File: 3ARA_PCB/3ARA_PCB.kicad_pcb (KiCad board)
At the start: 2 copper layers, 57 parts, among them J1 ST-LINK V2, J10 Encoder 2, J11 Encoder 3, J12 JUMP_1, J13 JUMP_2, J14 SPI 1, J15 UART 5, J2 Motor 1, J3 Hall 1, J4 Motor 2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

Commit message: Avance con el PCB
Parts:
- removed C14: 100nF, Capacitor_SMD:C_0805_2012Metric_Pad1.18x1.45mm_HandSolder
- removed C15: 1uF, Capacitor_SMD:C_0805_2012Metric_Pad1.18x1.45mm_HandSolder
- added C21: 1000uF, Capacitor_THT:CP_Radial_D10.0mm_P7.50mm, F.Cu at (184.1, 70.4)
- added D5: LED, LED_SMD:LED_0805_2012Metric_Pad1.15x1.40mm_HandSolder, F.Cu at (150.6, 78.1)
- added D6: LED, LED_SMD:LED_0805_2012Metric_Pad1.15x1.40mm_HandSolder, F.Cu at (150.6, 72.1)
- added J16: GPIO, Connector_PinHeader_2.54mm:PinHeader_2x05_P2.54mm_Vertical, F.Cu at (169.1, 88.5)
- added J9: DC Input, Connector_JST:JST_EH_B2B-EH-A_1x02_P2.50mm_Vertical, F.Cu at (154.2, 53.8)
- added L2: 100uH - optional, Inductor_THT:L_Axial_L7.0mm_D3.3mm_P12.70mm_Horizontal_Fastron_MICC, F.Cu at (181.1, 65.5)
- added R12: 1K, Resistor_SMD:R_0805_2012Metric_Pad1.20x1.40mm_HandSolder, F.Cu at (185.8, 94.8)
- added R13: 1K, Resistor_SMD:R_0805_2012Metric_Pad1.20x1.40mm_HandSolder, F.Cu at (185.8, 92.5)
- added R14: 1K, Resistor_SMD:R_0805_2012Metric_Pad1.20x1.40mm_HandSolder, F.Cu at (147.9, 72.1)
- C18, C19: value 0.1uF -> 100nF
- J1: footprint Connector_PinHeader_2.54mm:PinHeader_2x05_P2.54mm_Vertical -> Connector_IDC:IDC-Header_2x05_P2.54mm_Vertical
- J14: value SPI 1 -> I2C 1
- J3: value Hall 1 -> Hall 3; footprint Connector_PinHeader_2.54mm:PinHeader_1x03_P2.54mm_Vertical -> Connector_JST:JST_EH_B3B-EH-A_1x03_P2.50mm_Vertical
- J5: footprint Connector_PinHeader_2.54mm:PinHeader_1x03_P2.54mm_Vertical -> Connector_JST:JST_EH_B3B-EH-A_1x03_P2.50mm_Vertical
- J7: value Hall 3 -> Hall 1; footprint Connector_PinHeader_2.54mm:PinHeader_1x03_P2.54mm_Vertical -> Connector_JST:JST_EH_B3B-EH-A_1x03_P2.50mm_Vertical
- L1: footprint Inductor_THT:L_Axial_L7.0mm_D3.3mm_P12.70mm_Horizontal_Fastron_MICC -> Inductor_SMD:L_12x12mm_H6mm
- R1: value 47 -> 120
- moved J11 135.3 mm to (175.2, 141.5)
- moved J8 126.9 mm to (124.9, 141.5)
- moved J2 111.1 mm to (196.3, 109.0), turned to 90 degrees
- moved J14 99.2 mm to (196.3, 94.7), turned to 90 degrees
- moved L1 97.1 mm to (191.7, 59.2), turned to 90 degrees
- moved D4 96.4 mm to (165.9, 73.9), turned to 270 degrees
- moved J15 94.3 mm to (196.3, 79.0), turned to 90 degrees
- moved U2 90.4 mm to (117.8, 64.3)
- moved J10 79.3 mm to (150.0, 141.5), turned to 0 degrees
- moved SW2 73.0 mm to (166.8, 122.2)
- moved C5 68.5 mm to (158.8, 86.9), turned to 45 degrees
- moved J7 65.7 mm to (108.6, 127.8), turned to 270 degrees
- moved C3 65.7 mm to (166.5, 102.7)
- moved J6 64.9 mm to (196.3, 136.9), turned to 90 degrees
- moved J4 63.5 mm to (196.3, 122.5), turned to 90 degrees
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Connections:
- C16 pad 2: /VREF+ -> +3V3
- C17 pad 2: /VREF+ -> +3V3
- J1 pad 1: (no net) -> /NRST
- J1 pad 5: (no net) -> GND
- J1 pad 7: (no net) -> Net-(J1-Pad7)
- J1 pad 8: +3V3 -> (no net)
- J11 pad 2: (no net) -> /TIM3_CH1
- J11 pad 3: (no net) -> /TIM3_CH2
- J14 pad 1: /PB5_SPI_1_MOSI -> +3V3
- J14 pad 2: /PB4_SPI_1_MISO -> /PB7_I2C1_SDA
- J14 pad 3: /PA5_SPI_1_SCK -> /PB6_I2C1_SCL
- J2 pad 3: (no net) -> /MOTOR_1_L
- J3 pad 1: /HALL_1 -> /HALL_3
- J4 pad 2: (no net) -> /MOTOR_2_R
- J4 pad 3: (no net) -> /MOTOR_2_L
- J7 pad 1: /HALL_3 -> /HALL_1
- R1 pad 1: /VREF+ -> Net-(D5-Pad2)
- R1 pad 2: +3V3 -> Net-(J1-Pad7)
- R10 pad 1: /HALL_3 -> /HALL_1
- R8 pad 1: /HALL_1 -> /HALL_3
- U1 pad 1: (no net) -> /MOTOR_2_R
- U1 pad 18: /MOTOR_1_R -> /MOTOR_1_L
- U1 pad 21: /VREF+ -> +3V3
- U1 pad 22: /VREF+ -> +3V3
- U1 pad 29: (no net) -> /MOTOR_1_R
- U1 pad 3: (no net) -> /MOTOR_2_L
- U1 pad 30: /PA5_SPI_1_SCK -> (no net)
- U1 pad 31: (no net) -> /TIM3_CH1
- U1 pad 32: (no net) -> /TIM3_CH2
- U1 pad 38: (no net) -> /PE7
- U1 pad 41: (no net) -> /PE10
- U1 pad 42: (no net) -> /PE11
- U1 pad 51: (no net) -> /PB12
- U1 pad 52: (no net) -> /PB13
- U1 pad 53: (no net) -> /PB14
- U1 pad 90: /PB4_SPI_1_MISO -> (no net)
- U1 pad 91: /PB5_SPI_1_MOSI -> (no net)
- U1 pad 92: (no net) -> /PB6_I2C1_SCL
- U1 pad 93: (no net) -> /PB7_I2C1_SDA
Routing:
- net +3V3: track 0.00 -> 548.3 mm, vias 0 -> 2
- net /NRST: track 0.00 -> 109.8 mm
- net /TIM4_CH2: track 0.00 -> 93.4 mm, vias 0 -> 2
- net /TIM4_CH1: track 0.00 -> 88.6 mm, vias 0 -> 2
- net /MOTOR_3(PWM): track 0.00 -> 81.8 mm
- net /MOTOR_2_R: track 0.00 -> 76.4 mm, vias 0 -> 1
- net /MOTOR_2_L: track 0.00 -> 70.6 mm, vias 0 -> 1
- net /HALL_1: track 0.00 -> 69.3 mm
- net /PB7_I2C1_SDA: track 0.00 -> 66.6 mm, vias 0 -> 2
- net /MOTOR_3_R: track 0.00 -> 64.3 mm, vias 0 -> 2
- net /PC12_UART_5_Tx: track 0.00 -> 61.8 mm, vias 0 -> 2
- net /MOTOR_3_L: track 0.00 -> 60.9 mm, vias 0 -> 2
- net /TIM8_CH2: track 0.00 -> 60.4 mm, vias 0 -> 2
- net /PD2_UART_5_Rx: track 0.00 -> 59.6 mm, vias 0 -> 2
- net /TIM8_CH1: track 0.00 -> 58.5 mm, vias 0 -> 2
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- added copper zone on B.Cu, net GND
- added copper zone on F.Cu, net GND
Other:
- board outline added: 95 x 95 mm

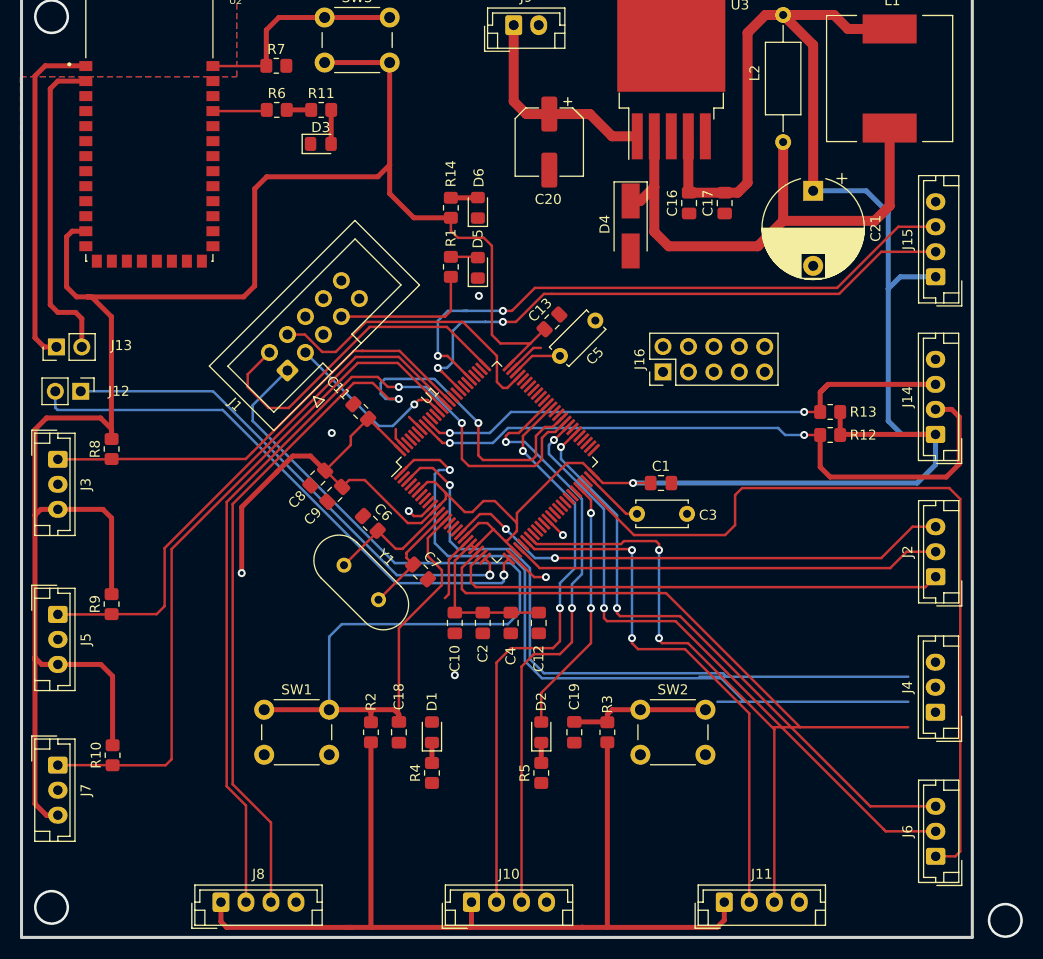
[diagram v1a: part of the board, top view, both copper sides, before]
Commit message: Agregado de gpios a pines
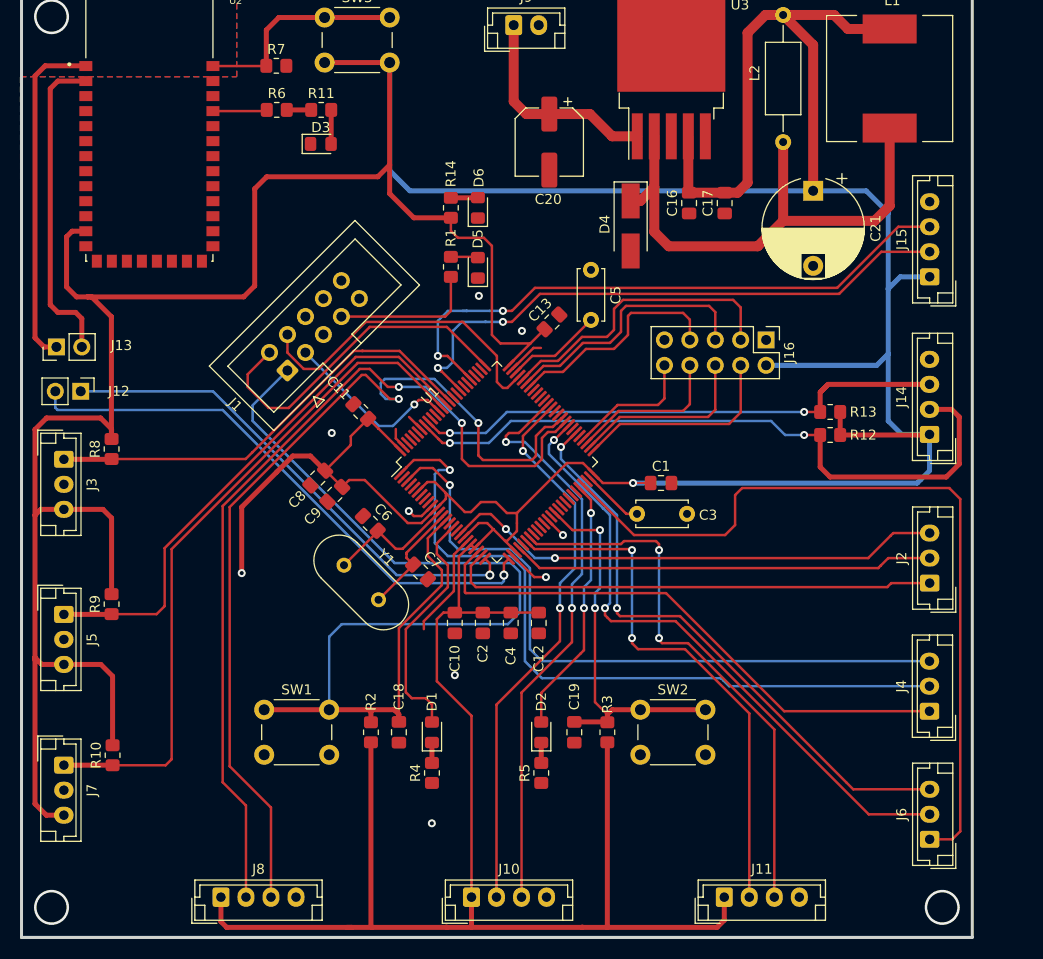
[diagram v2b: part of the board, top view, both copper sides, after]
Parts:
- moved J16 10.8 mm to (179.4, 85.3), turned to 270 degrees
- moved C5 4.75 mm to (161.9, 83.3), turned to 90 degrees
- moved J6 1.80 mm to (195.7, 135.2)
- moved J2 0.87 mm to (195.7, 109.6)
- moved J4 0.61 mm to (195.7, 122.4)
- moved J15 0.60 mm to (195.7, 79.0)
- moved J14 0.60 mm to (195.7, 94.7)
- moved J3 0.60 mm to (109.2, 97.2)
- moved J5 0.60 mm to (109.2, 112.7)
- moved J7 0.60 mm to (109.2, 127.8)
- moved J10 0.50 mm to (150.0, 141.0)
- moved J11 0.50 mm to (175.2, 141.0)
- moved J8 0.50 mm to (124.9, 141.0)
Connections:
- C19 pad 2: /PD15 -> /PE8
- D1 pad 2: /PE0 -> /PC1
- J16 pad 1: /PE7 -> GND
- J16 pad 10: +3V3 -> /PB15
- J16 pad 2: /PE10 -> +3V3
- J16 pad 3: /PE11 -> /PA12
- J16 pad 5: /PB13 -> /PA11
- J16 pad 6: GND -> /PB13
- J16 pad 7: (no net) -> /PA10
- J16 pad 8: (no net) -> /PB14
- J16 pad 9: /PB14 -> GND
- R3 pad 1: /PD15 -> /PE8
- SW2 pad 1: /PD15 -> /PE8
- U1 pad 16: (no net) -> /PC1
- U1 pad 38: /PE7 -> (no net)
- U1 pad 39: (no net) -> /PE8
- U1 pad 41: /PE10 -> (no net)
- U1 pad 42: /PE11 -> (no net)
- U1 pad 54: (no net) -> /PB15
- U1 pad 62: /PD15 -> (no net)
- U1 pad 69: (no net) -> /PA10
- U1 pad 70: (no net) -> /PA11
- U1 pad 71: (no net) -> /PA12
- U1 pad 97: /PE0 -> (no net)
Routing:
- net +3V3: track 548.3 -> 640.5 mm
- net /PE8: track 0.00 -> 38.5 mm, vias 0 -> 2
- net /PA12: track 0.00 -> 29.9 mm
- net /PA11: track 0.00 -> 26.3 mm
- net /PC1: track 0.00 -> 24.3 mm
- net /PA10: track 0.00 -> 22.4 mm
- net /PB12: track 0.00 -> 21.0 mm
- net /PB13: track 0.00 -> 18.5 mm
- net /PB14: track 0.00 -> 15.8 mm
- net /PD15: track 14.1 -> 0.00 mm
- net /PB15: track 0.00 -> 13.1 mm
- net Net-(C5-Pad1): track 5.09 -> 9.68 mm
- net GND: track 23.5 -> 27.5 mm, vias 8 -> 10
- net /TIM8_CH1: track 58.5 -> 55.6 mm
- net /SWDIO: track 29.9 -> 32.4 mm
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
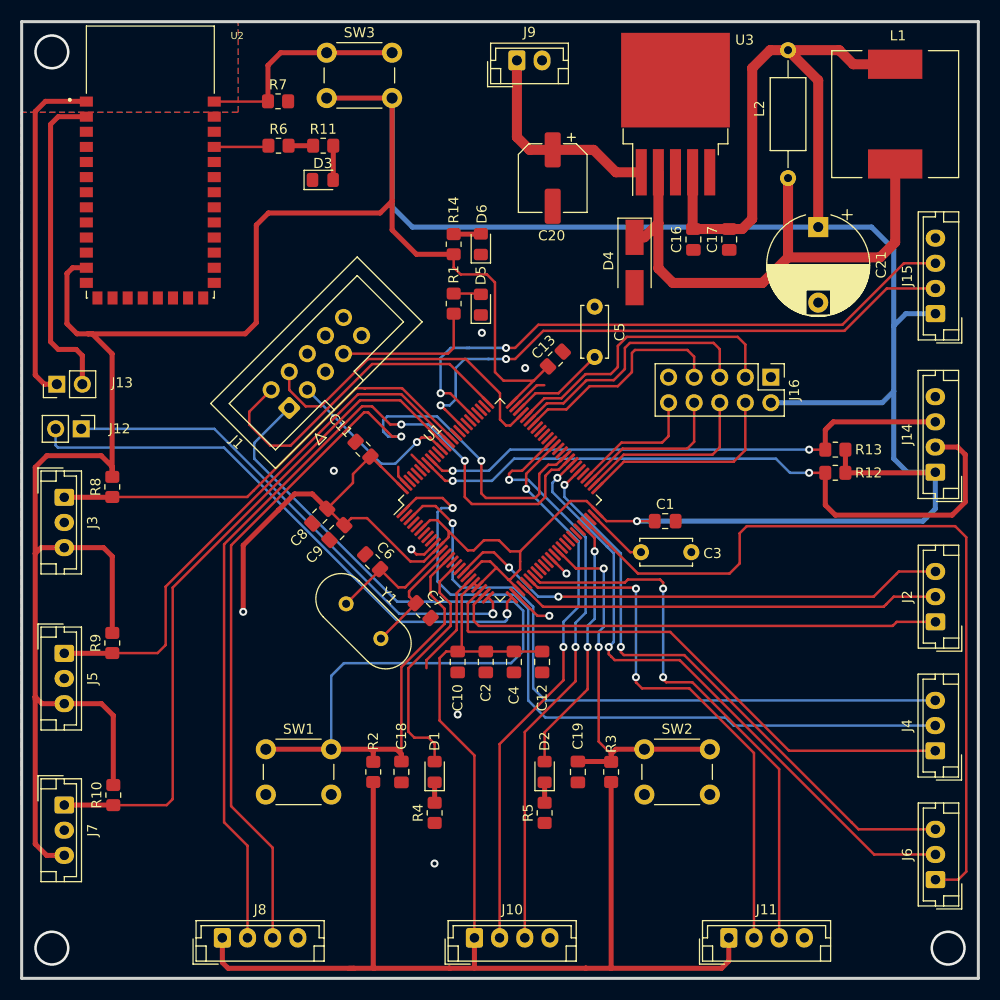
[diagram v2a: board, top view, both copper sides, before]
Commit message: Generación de la BOM
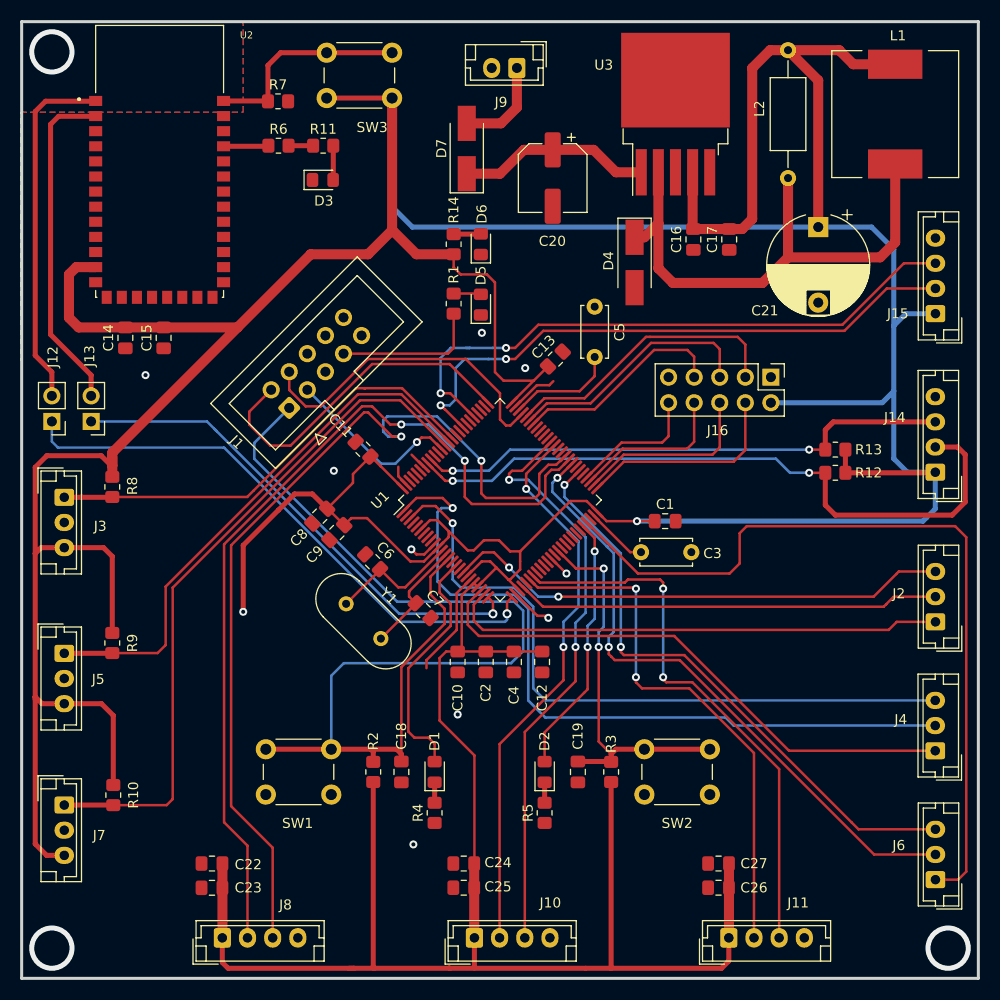
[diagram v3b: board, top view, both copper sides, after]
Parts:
- added C14: 100nF, Capacitor_SMD:C_0805_2012Metric_Pad1.18x1.45mm_HandSolder, F.Cu at (115.3, 81.4)
- added C15: 1uF, Capacitor_SMD:C_0805_2012Metric_Pad1.18x1.45mm_HandSolder, F.Cu at (119.1, 81.4)
- added C22: 100nF, Capacitor_SMD:C_0805_2012Metric_Pad1.18x1.45mm_HandSolder, F.Cu at (123.9, 133.6)
- added C23: 1uF, Capacitor_SMD:C_0805_2012Metric_Pad1.18x1.45mm_HandSolder, F.Cu at (123.9, 136.0)
- added C24: 1uF, Capacitor_SMD:C_0805_2012Metric_Pad1.18x1.45mm_HandSolder, F.Cu at (148.9, 133.6)
- added C25: 100nF, Capacitor_SMD:C_0805_2012Metric_Pad1.18x1.45mm_HandSolder, F.Cu at (148.9, 136.0)
- added C26: 1uF, Capacitor_SMD:C_0805_2012Metric_Pad1.18x1.45mm_HandSolder, F.Cu at (174.2, 136.0)
- added C27: 100nF, Capacitor_SMD:C_0805_2012Metric_Pad1.18x1.45mm_HandSolder, F.Cu at (174.2, 133.6)
- added D7: MBR360, Diode_SMD:D_SMA_Handsoldering, F.Cu at (149.2, 62.6)
- moved J13 5.03 mm to (111.9, 89.7), turned to 180 degrees
- moved J12 3.01 mm to (108.0, 89.7), turned to 180 degrees
- moved U2 0.93 mm to (118.7, 64.2)
- moved J9 0.75 mm to (154.2, 54.6), turned to 180 degrees
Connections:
- J12 pad 1: /PA2(Tx) -> /PA3(Rx)
- J12 pad 2: /PA3(Rx) -> /HC05_TX
- J13 pad 1: /HC05_TX -> /PA2(Tx)
- J9 pad 1: +12V -> Net-(D7-Pad2)
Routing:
- net +3V3: track 640.5 -> 660.9 mm
- net Net-(D7-Pad2): track 0.00 -> 9.55 mm
- net +12V: track 21.4 -> 19.2 mm
- net /HC05_RX: track 32.0 -> 33.5 mm
- net /PA11: track 26.3 -> 25.1 mm
- net /PA12: track 29.9 -> 28.6 mm
- net /HC05_TX: track 34.2 -> 35.4 mm
- net Net-(C5-Pad1): track 9.68 -> 10.8 mm
- net /PA10: track 22.4 -> 21.3 mm
- net GND: track 27.5 -> 28.6 mm, vias 10 -> 11
- net /PA3(Rx): track 56.2 -> 57.1 mm
- net Net-(R7-Pad1): track 21.8 -> 20.9 mm
- net Net-(R6-Pad1): track 5.43 -> 4.65 mm

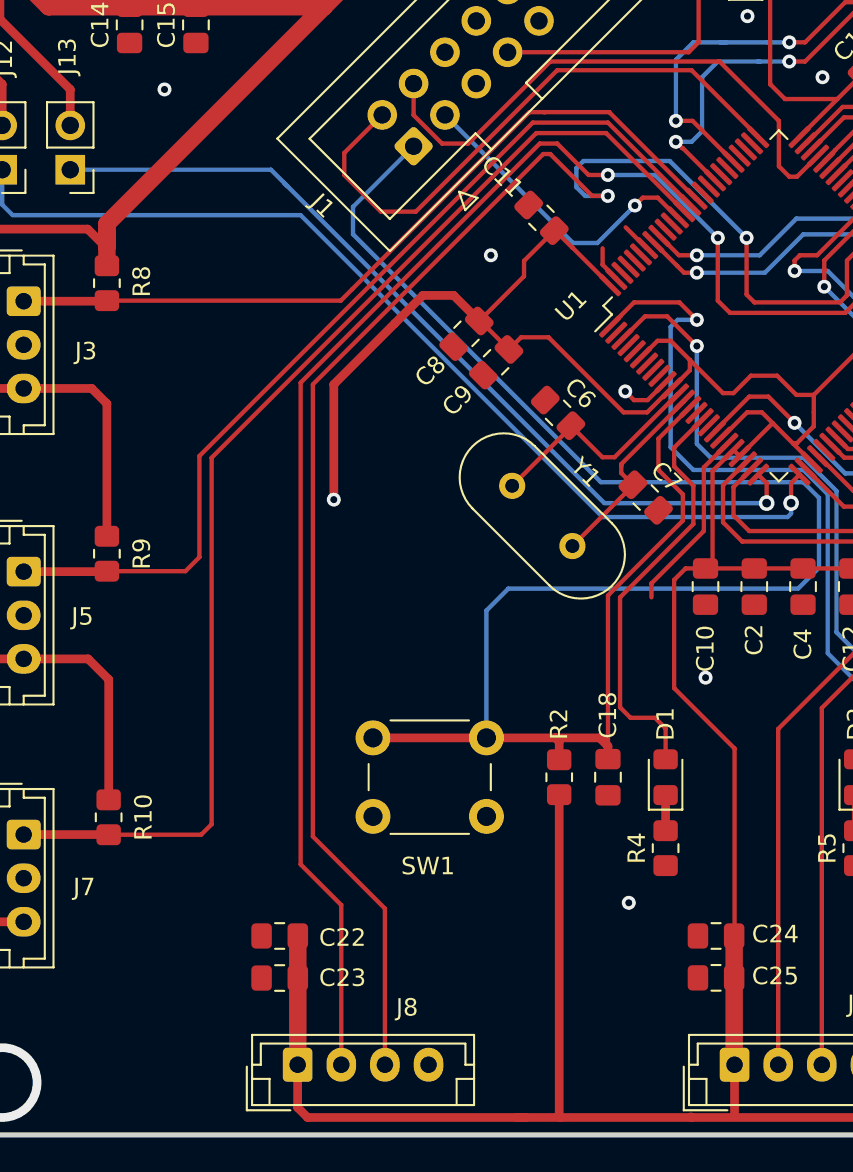
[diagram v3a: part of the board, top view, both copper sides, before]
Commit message: Agregado de R pull down a boot 0 y capacitores en alimentacion
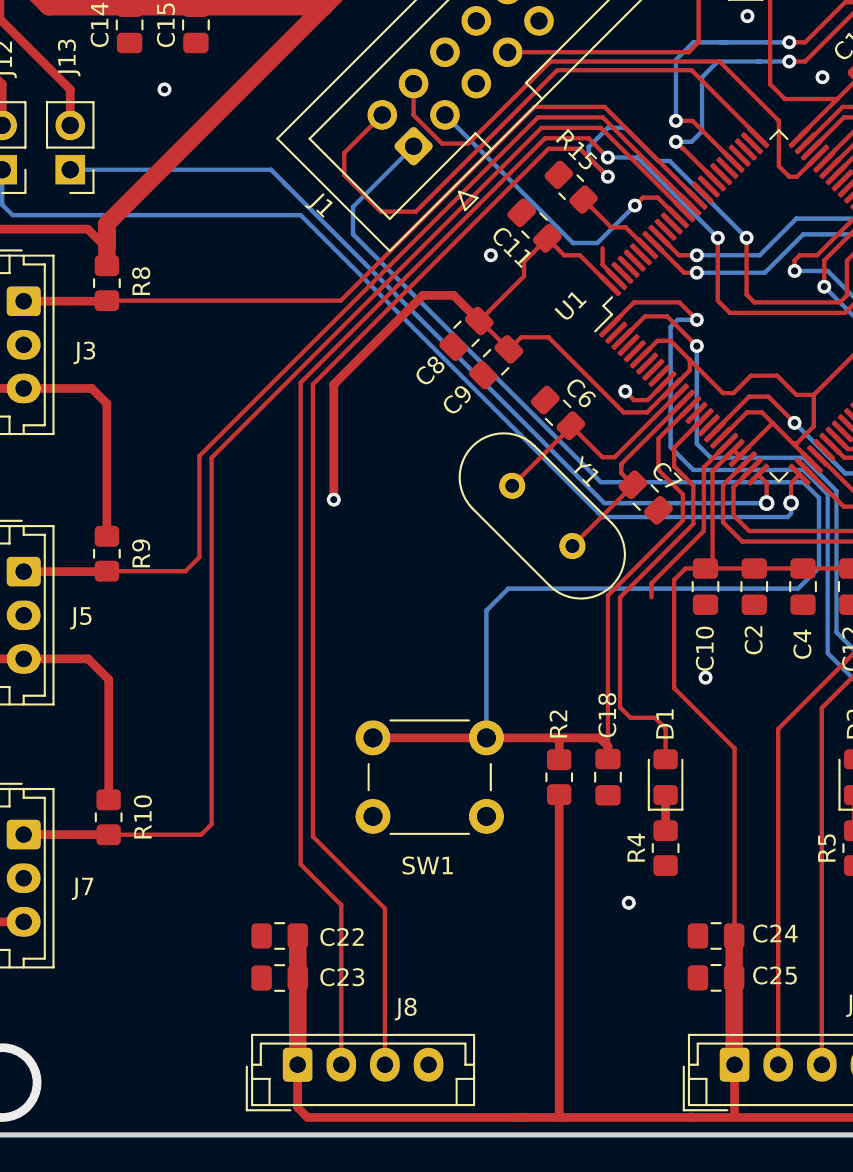
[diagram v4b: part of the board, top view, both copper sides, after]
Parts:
- added R15: 1K, Resistor_SMD:R_0805_2012Metric_Pad1.20x1.40mm_HandSolder, F.Cu at (140.6, 90.7)
- moved C11 0.60 mm to (138.5, 92.9)
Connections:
- U1 pad 94: GND -> Net-(R15-Pad2)
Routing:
- net Net-(R15-Pad2): track 0.00 -> 4.80 mm
- net GND: track 28.6 -> 26.8 mm
- net /TIM4_CH2: track 93.8 -> 93.0 mm
